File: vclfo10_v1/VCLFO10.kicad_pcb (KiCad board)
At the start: 2 copper layers, 76 x 100 mm, 139 parts, among them J1 Conn_02x05_Odd_Even, Q1 BC547, Q2 BC547, U1 LM358, U2 LM358, U3 LM7805_TO220, U4 ED_VCLFO10, U5 LM358, U6 TL072, U7 TL072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

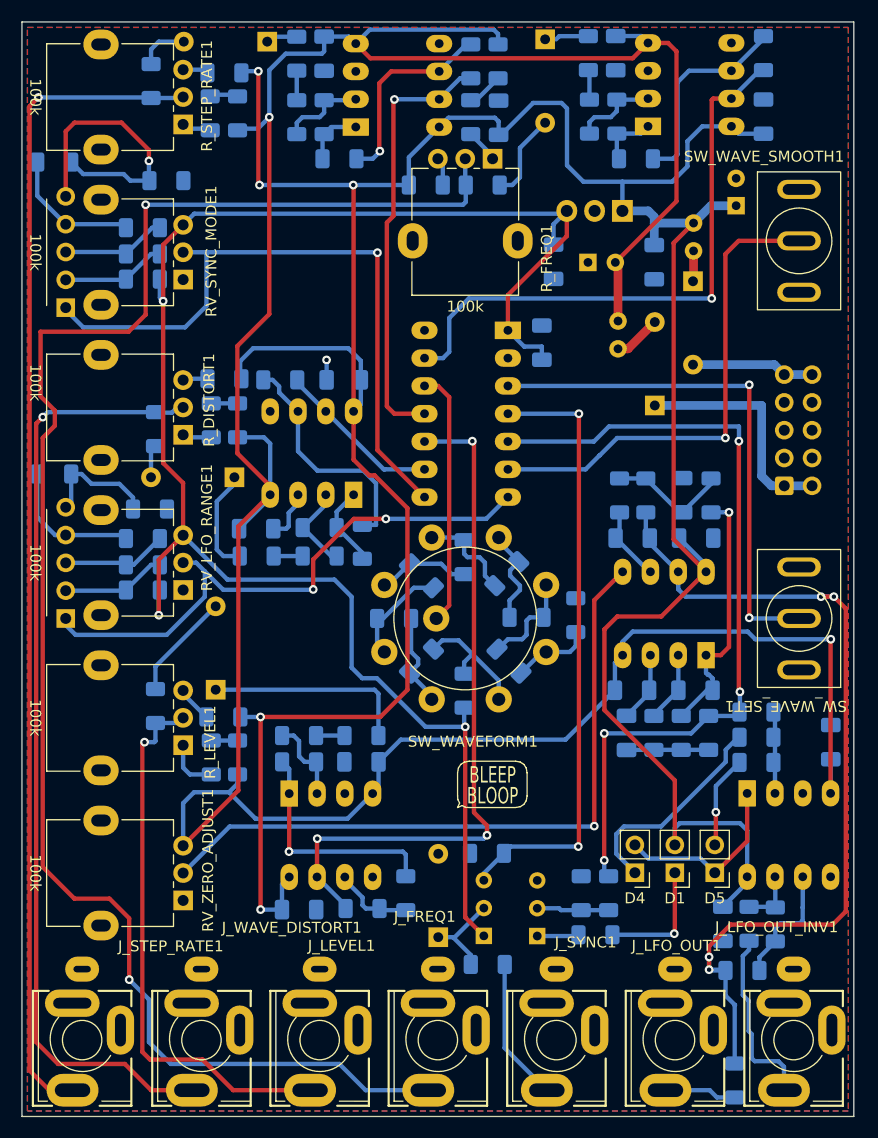
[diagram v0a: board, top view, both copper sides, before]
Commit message: Moved pcb files to sub folder
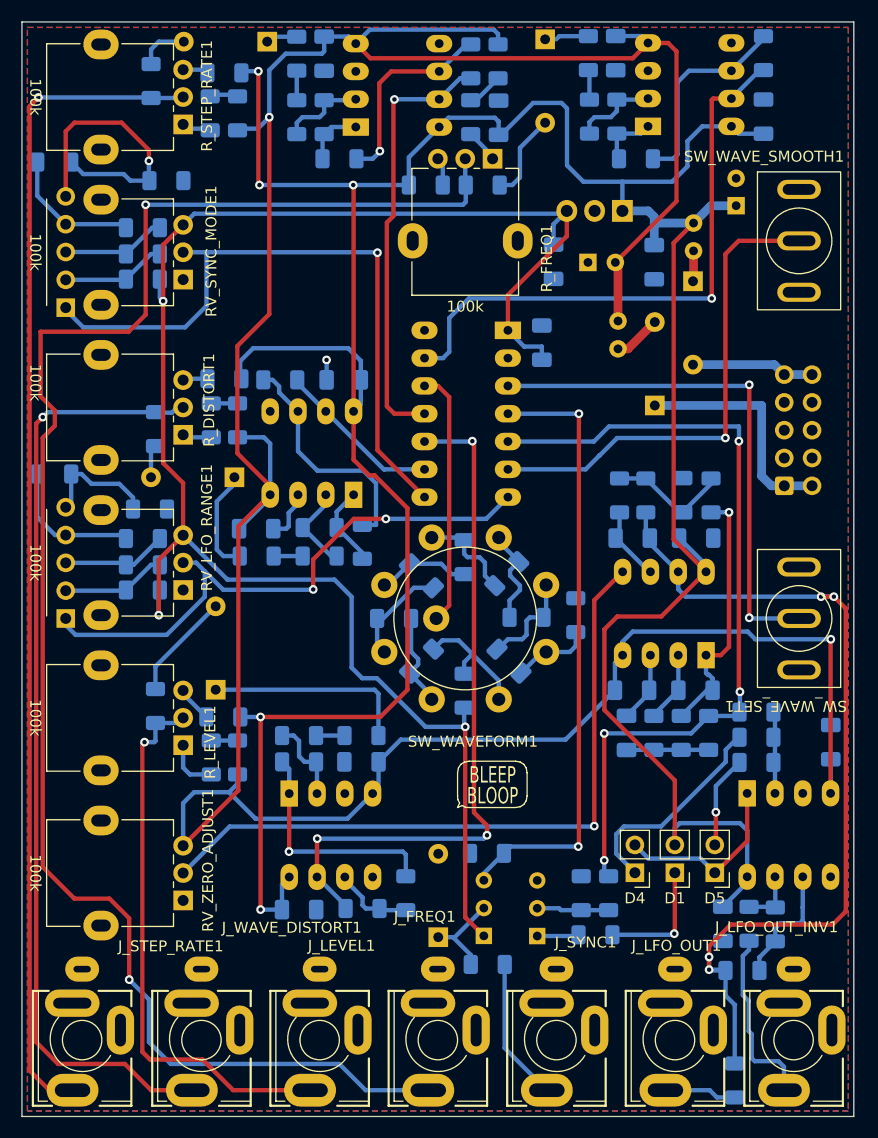
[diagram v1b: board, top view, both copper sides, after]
